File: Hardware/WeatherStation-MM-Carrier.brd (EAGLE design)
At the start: 67.3 x 58.4 mm, 155 parts, among them J11 microSD, J13 RJ11 - WIND, J15 MICROMOD-2222-C, J2 JTAG, J3 QWIIC_RIGHT_ANGLE, J7 RJ11 - RAIN, U1 BME280, U2 VEML6075, U3 AS3935, U5 AP7361C-33FGEUDFN-8

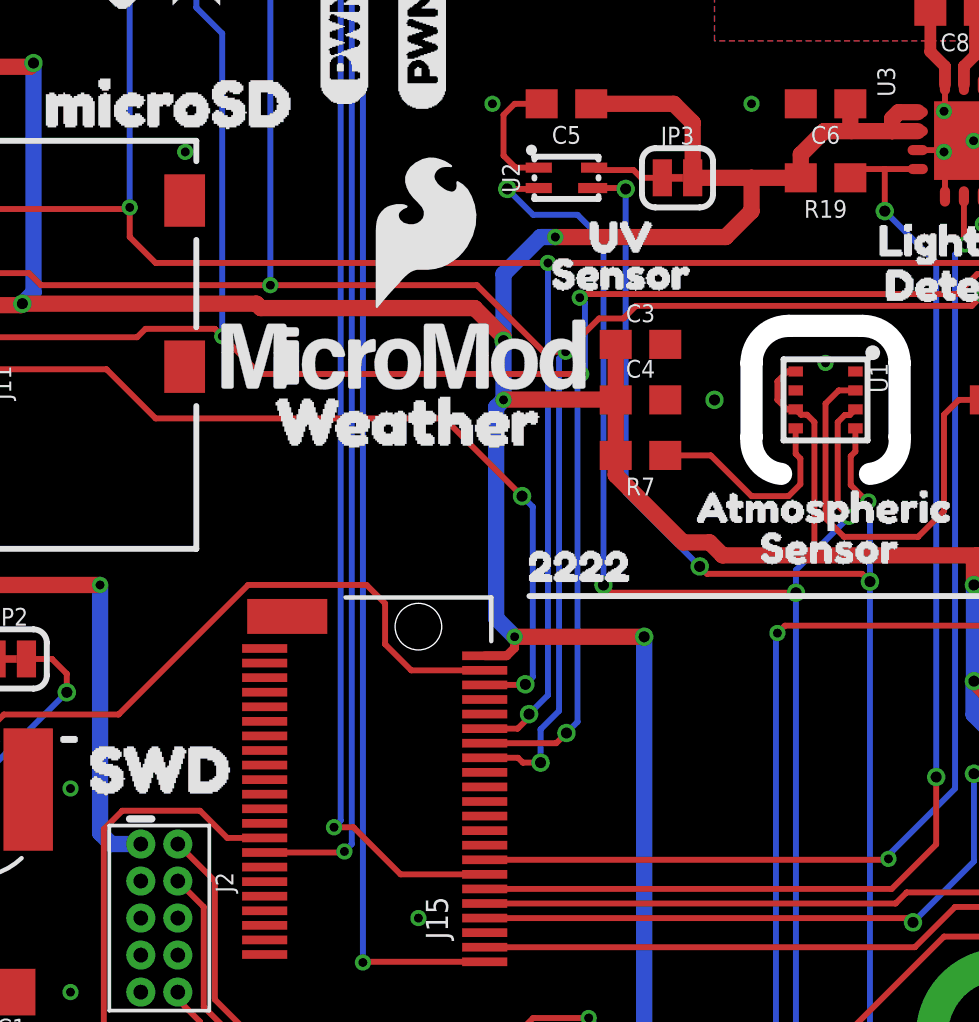
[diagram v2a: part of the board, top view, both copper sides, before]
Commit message: QC Double check changes
Added SWDIO test point, notes on VE jumper, measurements for standoffs, double check sparkle BOM, and DRC
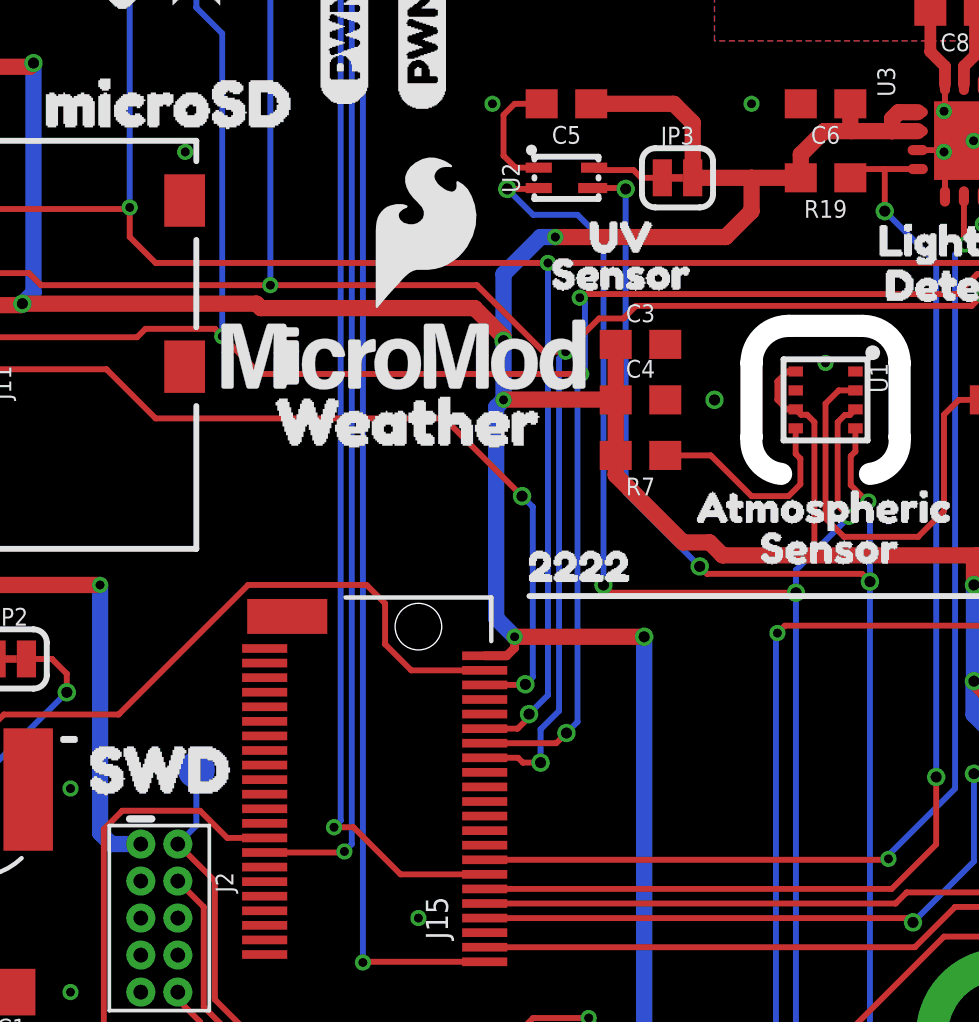
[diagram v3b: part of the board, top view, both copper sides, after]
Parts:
- added TP1: TEST-POINT3X5, SparkFun-Connectors:PAD.03X.05
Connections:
- net SWDIO: now also TP1.P$1
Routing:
- net SWDIO: track 7.97 -> 10.8 mm
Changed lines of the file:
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@@
 <?xml version="1.0" encoding="utf-8"?>
 <!DOCTYPE eagle SYSTEM "eagle.dtd">
-<eagle version="9.5.2">
+<eagle version="9.4.2">
 <drawing>
 <settings>
-<setting alwaysvectorfont="no"/>
+<setting alwaysvectorfont="yes"/>
 <setting verticaltext="up"/>
 </settings>
@@
 <layer number="45" name="Holes" color="7" fill="1" visible="yes" active="yes"/>
 <layer number="46" name="Milling" color="3" fill="1" visible="no" active="yes"/>
-<layer number="47" name="Measures" color="7" fill="1" visible="no" active="yes"/>
+<layer number="47" name="Measures" color="7" fill="1" visible="yes" active="yes"/>
 <layer number="48" name="Document" color="7" fill="1" visible="no" active="yes"/>
 <layer number="49" name="Reference" color="7" fill="1" visible="no" active="yes"/>
@@
 <layer number="95" name="Names" color="7" fill="1" visible="no" active="no"/>
 <layer number="96" name="Values" color="7" fill="1" visible="no" active="no"/>
-<layer number="2" name="Route2" color="1" fill="3" visible="no" active="no"/>
+<layer number="2" name="Route2" color="1" fill="3" visible="no" active="yes"/>
 <layer number="3" name="Route3" color="4" fill="3" visible="no" active="no"/>
 <layer number="4" name="Route4" color="1" fill="4" visible="no" active="no"/>
@@
 <layer number="13" name="Route13" color="4" fill="5" visible="no" active="no"/>
 <layer number="14" name="Route14" color="1" fill="6" visible="no" active="no"/>
-<layer number="15" name="Route15" color="4" fill="6" visible="no" active="no"/>
+<layer number="15" name="Route15" color="4" fill="6" visible="no" active="yes"/>
 <layer number="53" name="tGND_GNDA" color="7" fill="9" visible="no" active="no"/>
 <layer number="54" name="bGND_GNDA" color="1" fill="9" visible="no" active="no"/>
@@
 <text x="71.12" y="40.64" size="1.778" layer="48" font="vector" ratio="15">Selective Solder Nozzle Width:
 0.354331</text>
+<dimension x1="2.54" y1="55.88" x2="64.77" y2="55.88" x3="33.655" y3="60.96" textsize="1.778" textratio="15" layer="47" unit="inch"/>
+<dimension x1="64.77" y1="55.88" x2="64.77" y2="2.54" x3="74.93" y3="29.21" textsize="1.778" textratio="15" layer="47" unit="inch"/>
 </plain>
 <attributes>
@@
 </class>
 </classes>
-<designrules name="SparkFun-2-layer-FAB-LIMIT">
-<description language="en">&lt;b&gt;SparkFun 2 Layer Design Rule Checks - STANDARD/TIGHT/FAB-LIMIT&lt;/b&gt;
+<designrules name="SparkFun-4-layer-FAB-LIMIT">
+<description language="en">&lt;b&gt;EAGLE Design Rules&lt;/b&gt;
 &lt;p&gt;
-These rules have been curated by SparkFuns DFM commitee. After doing much research, communicating with our multiple fab houses, and getting quotes of various designs, we have compiled three DRU files.
-&lt;p&gt;
-&lt;b&gt;STANDARD:&lt;/b&gt; This is more of a &quot;best case scenario&quot; set of limitations. If your design has the space, and/or you have the time to work within these parameters, please do. Larger trace width and clearance makes for easier visual inspection of the PCB while troubleshooting (useful in production and to the end user). It also allows for better ability to hack a trace (if you are crazy enough to scrape away the mask and solder to a trace). Another thing to keep in mind is that more metal is just more robust.
-&lt;p&gt;
-&lt;b&gt;TIGHT:&lt;/b&gt; This is where cost comes into play. We have found that most fab houses begin to add extra charges when you go smaller than these specs. In some cases, going to less than 15 mil trace can increase the cost by 10%. (This is why we have set the min drill on this DRU to 15 mil) Same story for traces thinner than 7 mil. To avoid those extra charges, then stay within the rules of this DRU.
-&lt;p&gt;
-&lt;b&gt;FAB-LIMIT:&lt;/b&gt; These set of rules are at the very limit of most fab houses capabilities. You will pay more for these specs, and it should be used on designs that have a darned good reason to need 4 mil vias and 4 mil traces.
-&lt;p&gt;
-**NOTE Clearance, Distance, Sizes, and Restring are all set to different limits in each of these three DRU files. Please compare the files within the CAM job editor window of eagle to see all the numbers.
-&lt;p&gt;
-***NOTE, Please set your Net Classes to default (0mil for all settings), so that it won't effect the DRC when you run it with these settings.</description>
-<param name="layerSetup" value="(1*16)"/>
-<param name="mtCopper" value="0.035mm 0.035mm 0.035mm 0.035mm 0.035mm 0.035mm 0.035mm 0.035mm 0.035mm 0.035mm 0.035mm 0.035mm 0.035mm 0.035mm 0.035mm 0.035mm"/>
-<param name="mtIsolate" value="1.5mm 0.15mm 0.2mm 0.15mm 0.2mm 0.15mm 0.2mm 0.15mm 0.2mm 0.15mm 0.2mm 0.15mm 0.2mm 0.15mm 0.2mm"/>
-<param name="mdWireWire" value="4mil"/>
-<param name="mdWirePad" value="4mil"/>
-<param name="mdWireVia" value="4mil"/>
-<param name="mdPadPad" value="4mil"/>
-<param name="mdPadVia" value="4mil"/>
-<param name="mdViaVia" value="4mil"/>
-<param name="mdSmdPad" value="4mil"/>
-<param name="mdSmdVia" value="4mil"/>
-<param name="mdSmdSmd" value="4mil"/>
+The default Design Rules have been set to cover
+a wide range of applications. Your particular design
+may have different requirements, so please make the
+necessary adjustments and save your customized
+design rules under a new name.</description>
+<param name="layerSetup" value="(1*2*15*16)"/>
+<param name="mtCopper" value="0.035559375mm 0.035559375mm 0.035mm 0.035mm 0.035mm 0.035mm 0.035mm 0.035mm 0.035mm 0.035mm 0.035mm 0.035mm 0.035mm 0.035mm 0.035559375mm 0.035559375mm"/>
+<param name="mtIsolate" value="0.47751875mm 0.47751875mm 0.2mm 0.15mm 0.2mm 0.15mm 0.2mm 0.15mm 0.2mm 0.15mm 0.2mm 0.15mm 0.2mm 0.15mm 0.47751875mm"/>
+<param name="mdWireWire" value="5mil"/>
+<param name="mdWirePad" value="5mil"/>
+<param name="mdWireVia" value="5mil"/>
+<param name="mdPadPad" value="5mil"/>
+<param name="mdPadVia" value="5mil"/>
+<param name="mdViaVia" value="5mil"/>
+<param name="mdSmdPad" value="5mil"/>
+<param name="mdSmdVia" value="5mil"/>
+<param name="mdSmdSmd" value="5mil"/>
 <param name="mdViaViaSameLayer" value="8mil"/>
 <param name="mnLayersViaInSmd" value="2"/>
@@
 <element name="U$27" library="buzzard_labels (12)" package="CIPO0" value="" x="13.97" y="51.435" smashed="yes" rot="R90"/>
 <element name="U$50" library="buzzard_labels (12)" package="CIPO0" value="" x="13.97" y="51.562" smashed="yes" rot="MR90"/>
+<element name="TP1" library="SparkFun-Connectors" package="PAD.03X.05" value="TEST-POINT3X5" x="16.51" y="25.4" smashed="yes" rot="MR0"/>
 </elements>
 <signals>
@@
 <wire x1="28.321" y1="43.688" x2="27.051" y2="42.418" width="0.5588" layer="16"/>
 <via x="28.829" y="43.688" extent="1-16" drill="0.3048"/>
-<wire x1="37.2305" y1="45.7005" x2="37.25" y2="45.72" width="0.2032" layer="1"/>
 <wire x1="37.075" y1="37.775" x2="36.774" y2="37.775" width="0.2032" layer="1"/>
 <wire x1="36.774" y1="37.775" x2="36.449" y2="38.1" width="0.2032" layer="1"/>
@@
 <contactref element="J15" pad="23"/>
 <wire x1="18.855" y1="16.57" x2="18.101" y2="16.57" width="0.2032" layer="1"/>
+<contactref element="TP1" pad="P$1"/>
+<wire x1="15.875" y1="22.86" x2="16.51" y2="23.495" width="0.2032" layer="16"/>
+<wire x1="16.51" y1="23.495" x2="16.51" y2="25.4" width="0.2032" layer="16"/>
 </signal>
 <signal name="SWDCK">

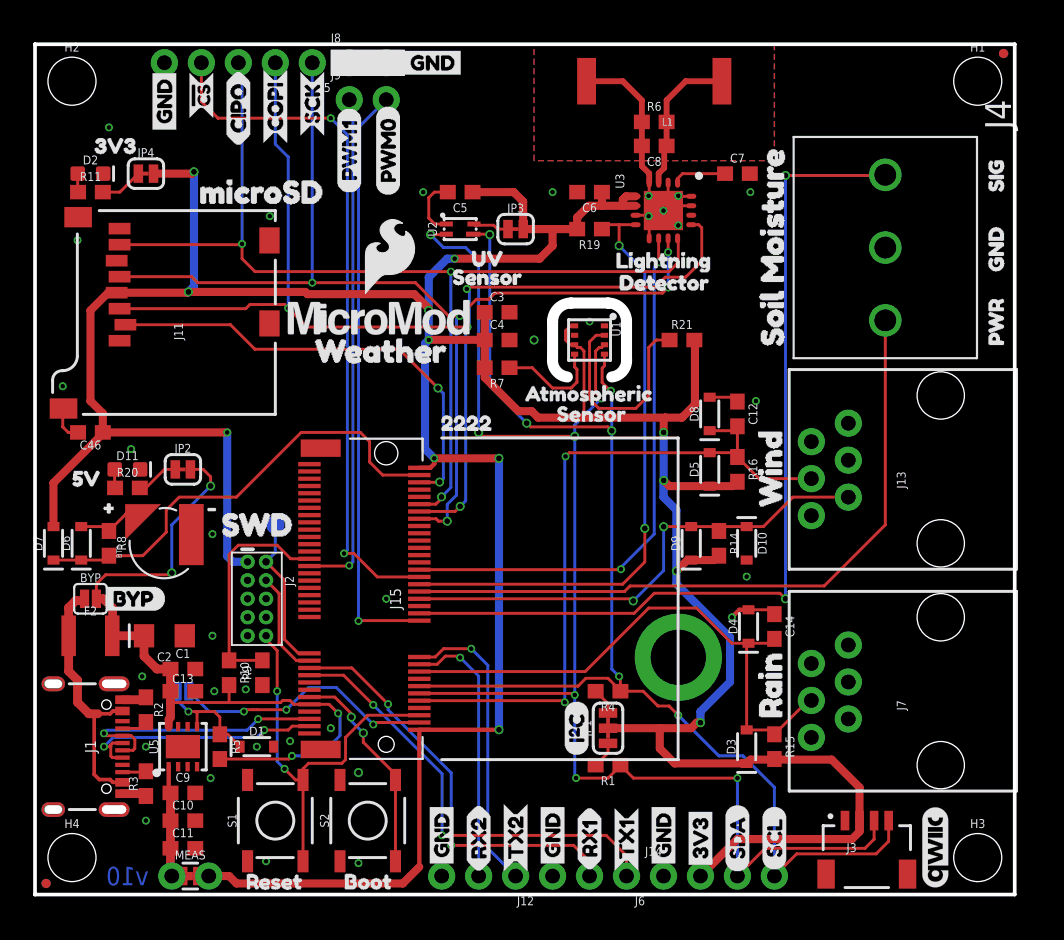
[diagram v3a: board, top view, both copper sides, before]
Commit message: Changed VE jumper silk
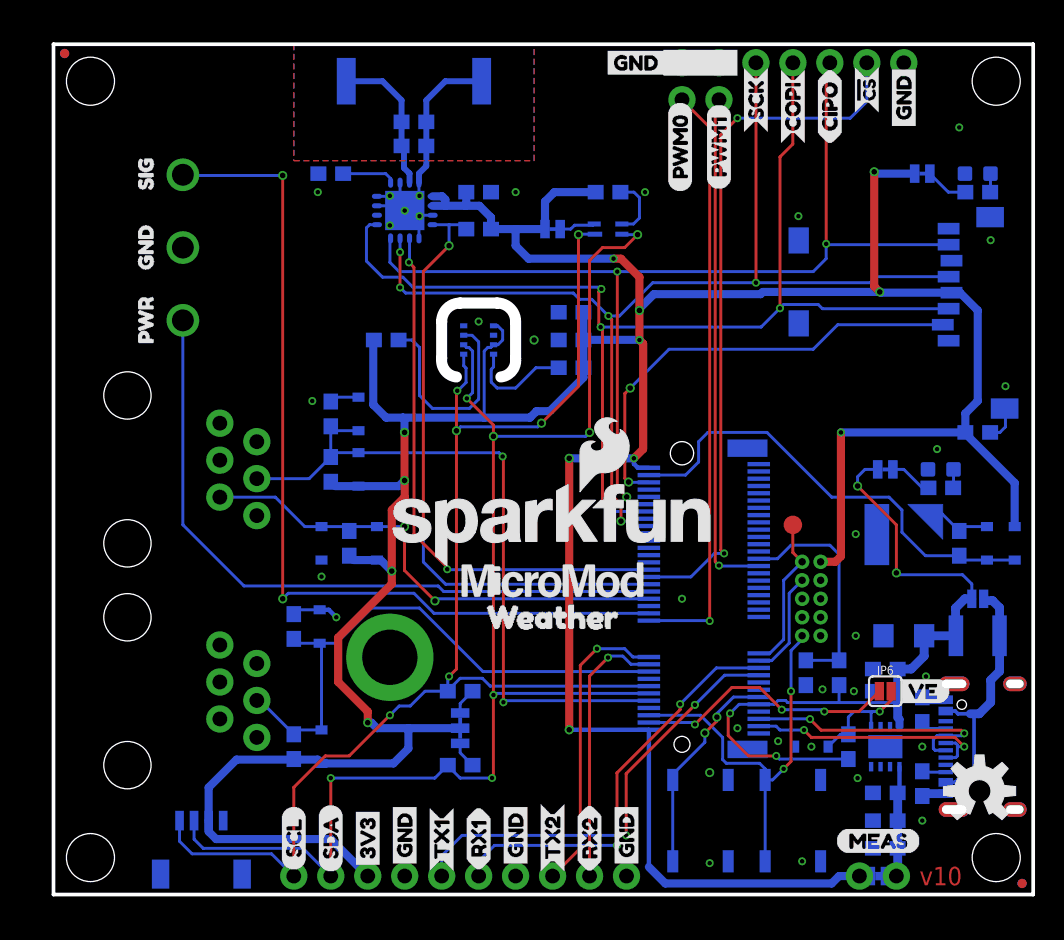
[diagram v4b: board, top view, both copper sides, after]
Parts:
- U$21: device buzzard_labels (11):3#3V_EN2 -> buzzard_labels (76):VE0
- moved FD1 67.1 mm to (67.8, 0.76), flipped to the bottom
- moved FD3 67.1 mm to (67.8, 0.76), flipped to the top
- moved D7 66.0 mm to (67.3, 24.1), flipped to the bottom
- moved U$18 65.3 mm to (66.9, 28.6), flipped to the bottom
- moved FD2 64.5 mm to (2.03, 57.8), flipped to the bottom
- moved FD4 64.5 mm to (2.03, 57.8), flipped to the top
- moved H2 63.5 mm to (66.0, 55.9), flipped to the bottom
- moved H4 63.5 mm to (66.0, 2.54), flipped to the bottom
- moved U$12 63.5 mm to (2.54, 36.8), flipped to the bottom
- moved U$13 63.5 mm to (2.54, 47.4), flipped to the bottom
- moved U$4 63.5 mm to (2.54, 41.9), flipped to the bottom
- moved D6 62.2 mm to (65.4, 24.1), flipped to the bottom
- moved U$1 62.2 mm to (65.4, 51.4), flipped to the bottom
- moved LOGO3 61.2 mm to (64.9, 7.11), flipped to the top
- moved BYP 61.0 mm to (64.8, 20.3), flipped to the bottom
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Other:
- outline, holes or cut-outs redrawn

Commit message: Update WeatherStation-MM-Carrier.brd
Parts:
- moved FD1 67.1 mm to (0.76, 0.76), flipped to the top
- moved FD3 67.1 mm to (0.76, 0.76), flipped to the bottom
- moved D7 66.0 mm to (1.27, 24.1), flipped to the top
- moved U$18 65.3 mm to (1.65, 28.6), flipped to the top
- moved FD2 64.5 mm to (66.5, 57.8), flipped to the top
- moved FD4 64.5 mm to (66.5, 57.8), flipped to the bottom
- moved H2 63.5 mm to (2.54, 55.9), flipped to the top
- moved H4 63.5 mm to (2.54, 2.54), flipped to the top
- moved U$12 63.5 mm to (66.0, 36.8), flipped to the top
- moved U$13 63.5 mm to (66.0, 47.4), flipped to the top
- moved U$4 63.5 mm to (66.0, 41.9), flipped to the top
- moved D6 62.2 mm to (3.17, 24.1), flipped to the top
- moved U$1 62.2 mm to (3.17, 51.4), flipped to the top
- moved LOGO3 61.2 mm to (3.68, 7.11), flipped to the bottom
- moved BYP 61.0 mm to (3.81, 20.3), flipped to the top
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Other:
- outline, holes or cut-outs redrawn
